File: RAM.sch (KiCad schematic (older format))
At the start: 169 parts, among them J2 JTAG_01x06, J3 Conn_01x03_Male, U10 W25Q128JVS, U11 TPS62823DLC, U12 TPS62823DLC, U13 TPS62823DLC, U14 TPS62823DLC, U15 TPS62823DLC, U16 TPS62823DLC, U2 XC7K160T-FFG676, U3 IS43TR16512B-125KBLI, U4 IS43TR16512B-125KBLI, U5 TPS51200DRC, U6 KSZ9031RNXCA, U7 TUSB1310ZAY, U8 TC358778XBG, U9 SiI9022A, Y1 ABM8G-25.000MHZ-18-D2Y-T, Y2 ABM8G-20.000MHZ-18-D2Y-T

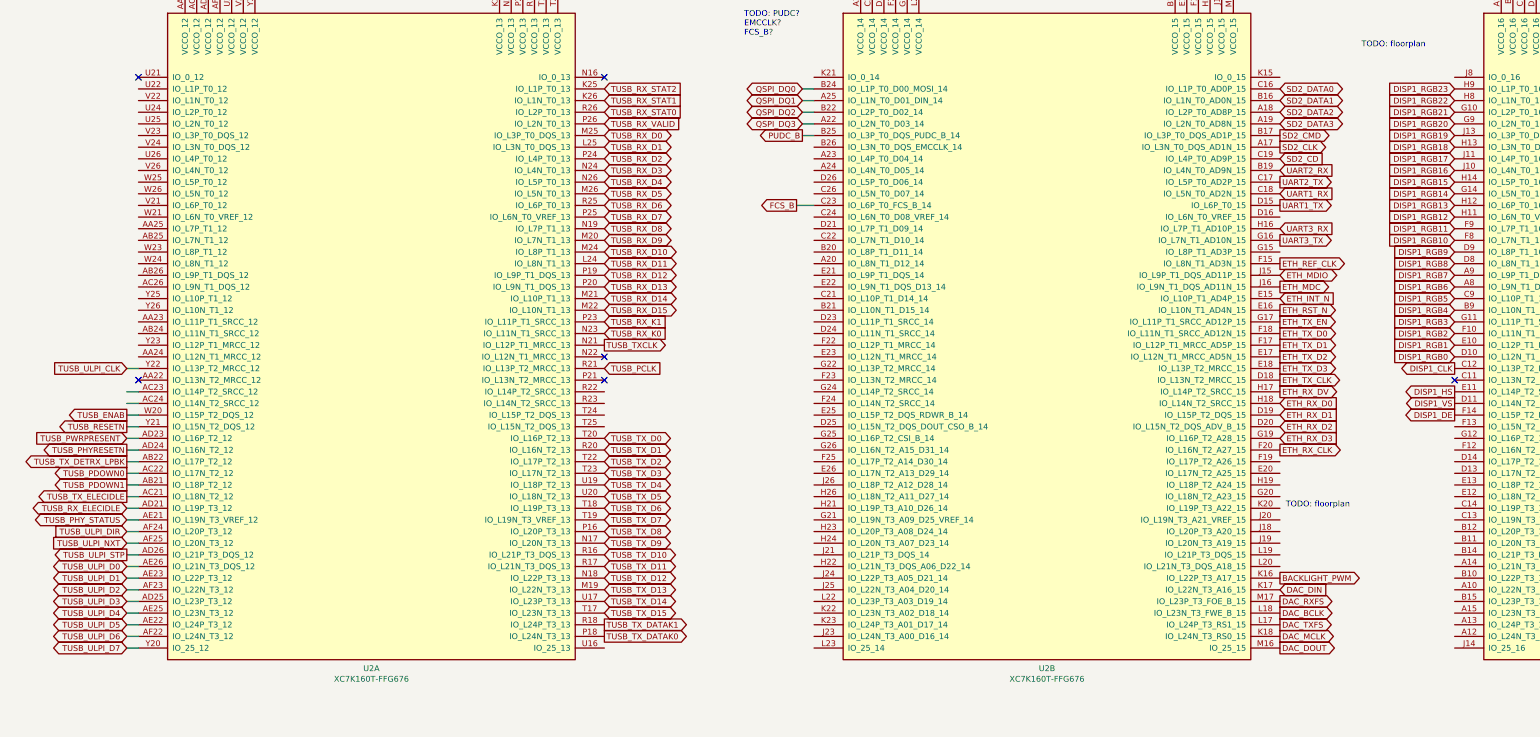
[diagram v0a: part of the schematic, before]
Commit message: more routing, esp. ethernet
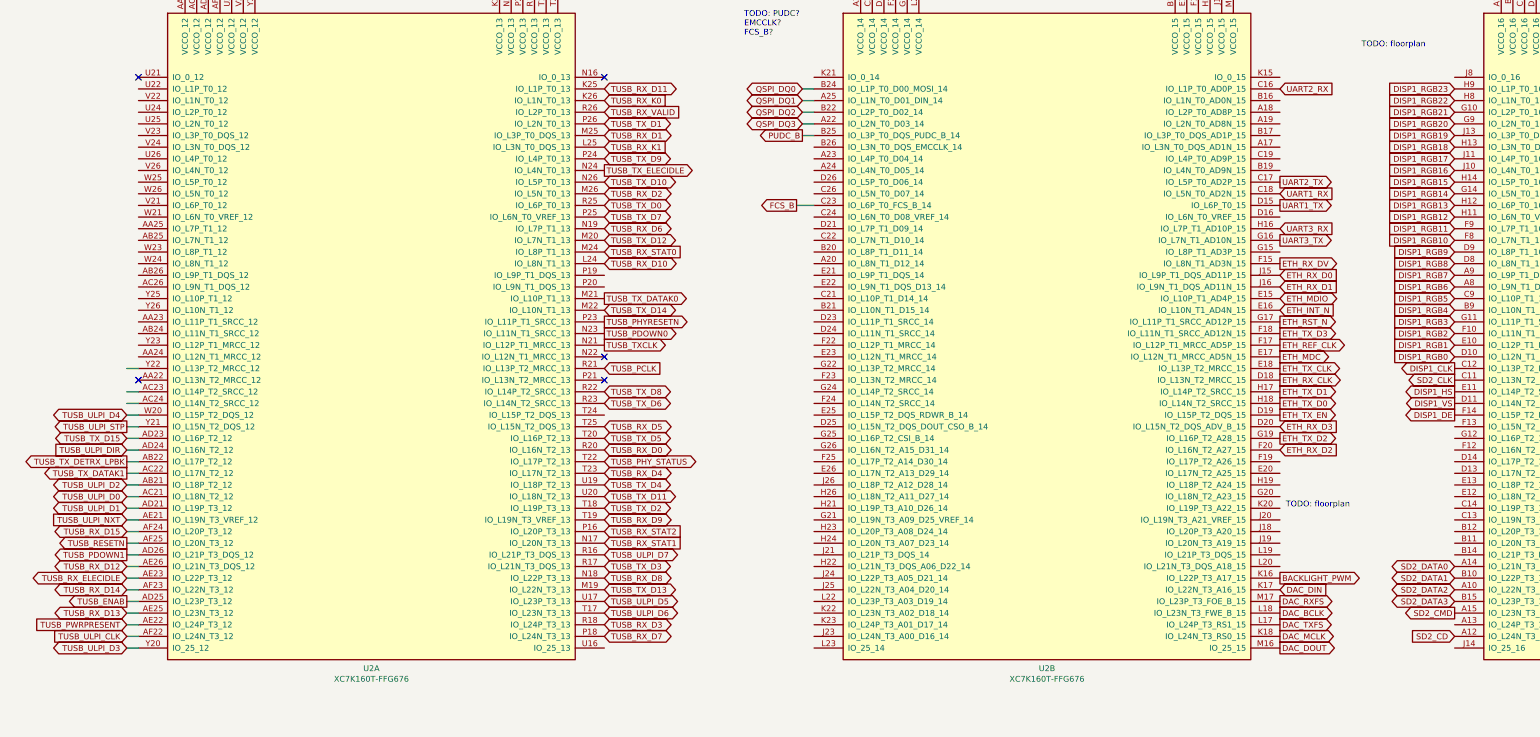
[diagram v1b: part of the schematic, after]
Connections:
- net ETH_INT_N: now also U2.E16 (IO_L10N_T1_AD4N_15); no longer U2.E15 (IO_L10P_T1_AD4P_15)
- net ETH_MDC: now also U2.E17 (IO_L12N_T1_MRCC_AD5N_15); no longer U2.J16 (IO_L9N_T1_DQS_AD11N_15)
- net ETH_MDIO: now also U2.E15 (IO_L10P_T1_AD4P_15); no longer U2.J15 (IO_L9P_T1_DQS_AD11P_15)
- net ETH_REF_CLK: now also U2.F17 (IO_L12P_T1_MRCC_AD5P_15); no longer U2.F15 (IO_L8N_T1_AD3N_15)
- net ETH_RST_N: now also U2.G17 (IO_L11P_T1_SRCC_AD12P_15); no longer U2.E16 (IO_L10N_T1_AD4N_15)
- net ETH_RX_CLK: now also U2.D18 (IO_L13N_T2_MRCC_15); no longer U2.F20 (IO_L16N_T2_A27_15)
- net ETH_RX_D0: now also U2.J15 (IO_L9P_T1_DQS_AD11P_15); no longer U2.H18 (IO_L14N_T2_SRCC_15)
- net ETH_RX_D1: now also U2.J16 (IO_L9N_T1_DQS_AD11N_15); no longer U2.D19 (IO_L15P_T2_DQS_15)
- net ETH_RX_D2: now also U2.F20 (IO_L16N_T2_A27_15); no longer U2.D20 (IO_L15N_T2_DQS_ADV_B_15)
- net ETH_RX_D3: now also U2.D20 (IO_L15N_T2_DQS_ADV_B_15); no longer U2.G19 (IO_L16P_T2_A28_15)
- net ETH_RX_DV: now also U2.F15 (IO_L8N_T1_AD3N_15); no longer U2.H17 (IO_L14P_T2_SRCC_15)
- net ETH_TX_CLK: now also U2.E18 (IO_L13P_T2_MRCC_15); no longer U2.D18 (IO_L13N_T2_MRCC_15)
- net ETH_TX_D0: now also U2.H18 (IO_L14N_T2_SRCC_15); no longer U2.F18 (IO_L11N_T1_SRCC_AD12N_15)
- net ETH_TX_D1: now also U2.H17 (IO_L14P_T2_SRCC_15); no longer U2.F17 (IO_L12P_T1_MRCC_AD5P_15)
- net ETH_TX_D2: now also U2.G19 (IO_L16P_T2_A28_15); no longer U2.E17 (IO_L12N_T1_MRCC_AD5N_15)
- net ETH_TX_D3: now also U2.F18 (IO_L11N_T1_SRCC_AD12N_15); no longer U2.E18 (IO_L13P_T2_MRCC_15)
- net ETH_TX_EN: now also U2.D19 (IO_L15P_T2_DQS_15); no longer U2.G17 (IO_L11P_T1_SRCC_AD12P_15)
- net SD2_CD: now also U2.A12 (IO_L24N_T3_16); no longer U2.C19 (IO_L4P_T0_AD9P_15)
- net SD2_CLK: now also U2.C11 (IO_L13N_T2_MRCC_16); no longer U2.A17 (IO_L3N_T0_DQS_AD1N_15)
- net SD2_CMD: now also U2.A15 (IO_L23N_T3_16); no longer U2.B17 (IO_L3P_T0_DQS_AD1P_15)
- net SD2_DATA0: now also U2.A14 (IO_L21N_T3_DQS_16); no longer U2.C16 (IO_L1P_T0_AD0P_15)
- net SD2_DATA1: now also U2.B10 (IO_L22P_T3_16); no longer U2.B16 (IO_L1N_T0_AD0N_15)
- net SD2_DATA2: now also U2.A10 (IO_L22N_T3_16); no longer U2.A18 (IO_L2P_T0_AD8P_15)
- net SD2_DATA3: now also U2.B15 (IO_L23P_T3_16); no longer U2.A19 (IO_L2N_T0_AD8N_15)
- net TUSB_ENAB: now also U2.AD25 (IO_L23P_T3_12); no longer U2.W20 (IO_L15P_T2_DQS_12)
- net TUSB_PDOWN0: now also U2.N23 (IO_L11N_T1_SRCC_13); no longer U2.AC22 (IO_L17N_T2_12)
- net TUSB_PDOWN1: now also U2.AD26 (IO_L21P_T3_DQS_12); no longer U2.AB21 (IO_L18P_T2_12)
- net TUSB_PHYRESETN: now also U2.P23 (IO_L11P_T1_SRCC_13); no longer U2.AD24 (IO_L16N_T2_12)
- net TUSB_PHY_STATUS: now also U2.T22 (IO_L17P_T2_13); no longer U2.AE21 (IO_L19N_T3_VREF_12)
- net TUSB_PWRPRESENT: now also U2.AE22 (IO_L24P_T3_12); no longer U2.AD23 (IO_L16P_T2_12)
- net TUSB_RESETN: now also U2.AF25 (IO_L20N_T3_12); no longer U2.Y21 (IO_L15N_T2_DQS_12)
- net TUSB_RX_D0: now also U2.R20 (IO_L16N_T2_13); no longer U2.M25 (IO_L3P_T0_DQS_13)
- net TUSB_RX_D1: now also U2.M25 (IO_L3P_T0_DQS_13); no longer U2.L25 (IO_L3N_T0_DQS_13)
- net TUSB_RX_D10: now also U2.L24 (IO_L8N_T1_13); no longer U2.M24 (IO_L8P_T1_13)
- net TUSB_RX_D11: now also U2.K25 (IO_L1P_T0_13); no longer U2.L24 (IO_L8N_T1_13)
- net TUSB_RX_D12: now also U2.AE26 (IO_L21N_T3_DQS_12); no longer U2.P19 (IO_L9P_T1_DQS_13)
- net TUSB_RX_D13: now also U2.AE25 (IO_L23N_T3_12); no longer U2.P20 (IO_L9N_T1_DQS_13)
- net TUSB_RX_D14: now also U2.AF23 (IO_L22N_T3_12); no longer U2.M21 (IO_L10P_T1_13)
- net TUSB_RX_D15: now also U2.AF24 (IO_L20P_T3_12); no longer U2.M22 (IO_L10N_T1_13)
- net TUSB_RX_D2: now also U2.M26 (IO_L5N_T0_13); no longer U2.P24 (IO_L4P_T0_13)
- net TUSB_RX_D3: now also U2.R18 (IO_L24P_T3_13); no longer U2.N24 (IO_L4N_T0_13)
- net TUSB_RX_D4: now also U2.T23 (IO_L17N_T2_13); no longer U2.N26 (IO_L5P_T0_13)
- net TUSB_RX_D5: now also U2.T25 (IO_L15N_T2_DQS_13); no longer U2.M26 (IO_L5N_T0_13)
- net TUSB_RX_D6: now also U2.N19 (IO_L7P_T1_13); no longer U2.R25 (IO_L6P_T0_13)
- net TUSB_RX_D7: now also U2.P18 (IO_L24N_T3_13); no longer U2.P25 (IO_L6N_T0_VREF_13)
- net TUSB_RX_D8: now also U2.N18 (IO_L22P_T3_13); no longer U2.N19 (IO_L7P_T1_13)
- net TUSB_RX_D9: now also U2.T19 (IO_L19N_T3_VREF_13); no longer U2.M20 (IO_L7N_T1_13)
- net TUSB_RX_ELECIDLE: now also U2.AE23 (IO_L22P_T3_12); no longer U2.AD21 (IO_L19P_T3_12)
- net TUSB_RX_K0: now also U2.K26 (IO_L1N_T0_13); no longer U2.N23 (IO_L11N_T1_SRCC_13)
- net TUSB_RX_K1: now also U2.L25 (IO_L3N_T0_DQS_13); no longer U2.P23 (IO_L11P_T1_SRCC_13)
- net TUSB_RX_STAT0: now also U2.M24 (IO_L8P_T1_13); no longer U2.R26 (IO_L2P_T0_13)
- net TUSB_RX_STAT1: now also U2.N17 (IO_L20N_T3_13); no longer U2.K26 (IO_L1N_T0_13)
- net TUSB_RX_STAT2: now also U2.P16 (IO_L20P_T3_13); no longer U2.K25 (IO_L1P_T0_13)
- net TUSB_RX_VALID: now also U2.R26 (IO_L2P_T0_13); no longer U2.P26 (IO_L2N_T0_13)
- net TUSB_TX_D0: now also U2.R25 (IO_L6P_T0_13); no longer U2.T20 (IO_L16P_T2_13)
- net TUSB_TX_D1: now also U2.P26 (IO_L2N_T0_13); no longer U2.R20 (IO_L16N_T2_13)
- net TUSB_TX_D10: now also U2.N26 (IO_L5P_T0_13); no longer U2.R16 (IO_L21P_T3_DQS_13)
- net TUSB_TX_D11: now also U2.U20 (IO_L18N_T2_13); no longer U2.R17 (IO_L21N_T3_DQS_13)
- net TUSB_TX_D12: now also U2.M20 (IO_L7N_T1_13); no longer U2.N18 (IO_L22P_T3_13)
- net TUSB_TX_D14: now also U2.M22 (IO_L10N_T1_13); no longer U2.U17 (IO_L23P_T3_13)
- net TUSB_TX_D15: now also U2.AD23 (IO_L16P_T2_12); no longer U2.T17 (IO_L23N_T3_13)
- net TUSB_TX_D2: now also U2.T18 (IO_L19P_T3_13); no longer U2.T22 (IO_L17P_T2_13)
- net TUSB_TX_D3: now also U2.R17 (IO_L21N_T3_DQS_13); no longer U2.T23 (IO_L17N_T2_13)
- net TUSB_TX_D5: now also U2.T20 (IO_L16P_T2_13); no longer U2.U20 (IO_L18N_T2_13)
- net TUSB_TX_D6: now also U2.R23 (IO_L14N_T2_SRCC_13); no longer U2.T18 (IO_L19P_T3_13)
- net TUSB_TX_D7: now also U2.P25 (IO_L6N_T0_VREF_13); no longer U2.T19 (IO_L19N_T3_VREF_13)
- net TUSB_TX_D8: now also U2.R22 (IO_L14P_T2_SRCC_13); no longer U2.P16 (IO_L20P_T3_13)
- net TUSB_TX_D9: now also U2.P24 (IO_L4P_T0_13); no longer U2.N17 (IO_L20N_T3_13)
- net TUSB_TX_DATAK0: now also U2.M21 (IO_L10P_T1_13); no longer U2.P18 (IO_L24N_T3_13)
- net TUSB_TX_DATAK1: now also U2.AC22 (IO_L17N_T2_12); no longer U2.R18 (IO_L24P_T3_13)
- net TUSB_TX_ELECIDLE: now also U2.N24 (IO_L4N_T0_13); no longer U2.AC21 (IO_L18N_T2_12)
- net TUSB_ULPI_CLK: now also U2.AF22 (IO_L24N_T3_12); no longer U2.Y22 (IO_L13P_T2_MRCC_12)
- net TUSB_ULPI_D0: now also U2.AC21 (IO_L18N_T2_12); no longer U2.AE26 (IO_L21N_T3_DQS_12)
- net TUSB_ULPI_D1: now also U2.AD21 (IO_L19P_T3_12); no longer U2.AE23 (IO_L22P_T3_12)
- net TUSB_ULPI_D2: now also U2.AB21 (IO_L18P_T2_12); no longer U2.AF23 (IO_L22N_T3_12)
- net TUSB_ULPI_D3: now also U2.Y20 (IO_25_12); no longer U2.AD25 (IO_L23P_T3_12)
- net TUSB_ULPI_D4: now also U2.W20 (IO_L15P_T2_DQS_12); no longer U2.AE25 (IO_L23N_T3_12)
- net TUSB_ULPI_D5: now also U2.U17 (IO_L23P_T3_13); no longer U2.AE22 (IO_L24P_T3_12)
- net TUSB_ULPI_D6: now also U2.T17 (IO_L23N_T3_13); no longer U2.AF22 (IO_L24N_T3_12)
- net TUSB_ULPI_D7: now also U2.R16 (IO_L21P_T3_DQS_13); no longer U2.Y20 (IO_25_12)
- net TUSB_ULPI_DIR: now also U2.AD24 (IO_L16N_T2_12); no longer U2.AF24 (IO_L20P_T3_12)
- net TUSB_ULPI_NXT: now also U2.AE21 (IO_L19N_T3_VREF_12); no longer U2.AF25 (IO_L20N_T3_12)
- net TUSB_ULPI_STP: now also U2.Y21 (IO_L15N_T2_DQS_12); no longer U2.AD26 (IO_L21P_T3_DQS_12)
- net UART2_RX: now also U2.C16 (IO_L1P_T0_AD0P_15); no longer U2.B19 (IO_L4N_T0_AD9N_15)
- no-connect marks 23 -> 22
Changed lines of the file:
@@
 Text Notes 14800 14850 0    50   ~ 0
 TODO: bank 14 config pins
-Text GLabel 11300 2700 2    50   Output ~ 0
+Text GLabel 12800 4700 0    50   Output ~ 0
 SD2_CLK
-Text GLabel 11300 2600 2    50   Output ~ 0
+Text GLabel 12800 6700 0    50   Output ~ 0
 SD2_CMD
-Text GLabel 11300 2500 2    50   BiDi ~ 0
+Text GLabel 12800 6600 0    50   BiDi ~ 0
 SD2_DATA3
-Text GLabel 11300 2400 2    50   BiDi ~ 0
+Text GLabel 12800 6500 0    50   BiDi ~ 0
 SD2_DATA2
-Text GLabel 11300 2300 2    50   BiDi ~ 0
+Text GLabel 12800 6400 0    50   BiDi ~ 0
 SD2_DATA1
-Text GLabel 11300 2200 2    50   BiDi ~ 0
+Text GLabel 12800 6300 0    50   BiDi ~ 0
 SD2_DATA0
 Text GLabel 11300 6900 2    50   Output ~ 0
@@
 Wire Wire Line
 	18250 9950 18650 9950
-Text GLabel 11300 2900 2    50   Input ~ 0
+Text GLabel 11300 2200 2    50   Input ~ 0
 UART2_RX
 Text GLabel 11300 3000 2    50   Output ~ 0
@@
 Text GLabel 11300 3200 2    50   Output ~ 0
 UART1_TX
-Text GLabel 11300 2800 2    50   Input ~ 0
+Text GLabel 12800 6900 0    50   Input ~ 0
 SD2_CD
 Text GLabel 11300 3400 2    50   Input ~ 0
@@
 Wire Wire Line
 	38250 11900 38400 11900
-Text GLabel 11300 3700 2    50   Output ~ 0
+Text GLabel 11300 4400 2    50   Output ~ 0
 ETH_REF_CLK
-Text GLabel 11300 3800 2    50   BiDi ~ 0
+Text GLabel 11300 4000 2    50   BiDi ~ 0
 ETH_MDIO
-Text GLabel 11300 3900 2    50   Output ~ 0
+Text GLabel 11300 4500 2    50   Output ~ 0
 ETH_MDC
-Text GLabel 11300 4000 2    50   Input ~ 0
+Text GLabel 11300 4100 2    50   Input ~ 0
 ETH_INT_N
-Text GLabel 11300 4900 2    50   Input ~ 0
+Text GLabel 11300 3800 2    50   Input ~ 0
 ETH_RX_D0
-Text GLabel 11300 5000 2    50   Input ~ 0
+Text GLabel 11300 3900 2    50   Input ~ 0
 ETH_RX_D1
-Text GLabel 11300 5100 2    50   Input ~ 0
+Text GLabel 11300 5300 2    50   Input ~ 0
 ETH_RX_D2
-Text GLabel 11300 5200 2    50   Input ~ 0
+Text GLabel 11300 5100 2    50   Input ~ 0
 ETH_RX_D3
-Text GLabel 11300 4800 2    50   Output ~ 0
+Text GLabel 11300 3700 2    50   Output ~ 0
 ETH_RX_DV
-Text GLabel 11300 4300 2    50   Output ~ 0
+Text GLabel 11300 4900 2    50   Output ~ 0
 ETH_TX_D0
-Text GLabel 11300 4400 2    50   Output ~ 0
+Text GLabel 11300 4800 2    50   Output ~ 0
 ETH_TX_D1
-Text GLabel 11300 4500 2    50   Output ~ 0
+Text GLabel 11300 5200 2    50   Output ~ 0
 ETH_TX_D2
-Text GLabel 11300 4600 2    50   Output ~ 0
+Text GLabel 11300 4300 2    50   Output ~ 0
 ETH_TX_D3
-Text GLabel 11300 4700 2    50   Output ~ 0
+Text GLabel 11300 4600 2    50   Output ~ 0
 ETH_TX_CLK
-Text GLabel 11300 4200 2    50   Output ~ 0
+Text GLabel 11300 5000 2    50   Output ~ 0
 ETH_TX_EN
-Text GLabel 11300 4100 2    50   Output ~ 0
+Text GLabel 11300 4200 2    50   Output ~ 0
 ETH_RST_N
 Text GLabel 35450 11600 0    50   Input ~ 0
@@
 Wire Wire Line
 	35450 11600 35650 11600
-Text GLabel 11300 5300 2    50   Output ~ 0
+Text GLabel 11300 4700 2    50   Output ~ 0
 ETH_RX_CLK
 Text Notes 11350 5800 0    50   ~ 0
@@
 Wire Wire Line
 	5100 21700 4950 21700
-Text GLabel 5500 5200 2    50   BiDi ~ 0
+Text GLabel 5500 3200 2    50   BiDi ~ 0
 TUSB_TX_D0
-Text GLabel 5500 5300 2    50   BiDi ~ 0
+Text GLabel 5500 2500 2    50   BiDi ~ 0
 TUSB_TX_D1
-Text GLabel 5500 5400 2    50   BiDi ~ 0
+Text GLabel 5500 5800 2    50   BiDi ~ 0
 TUSB_TX_D2
-Text GLabel 5500 5500 2    50   BiDi ~ 0
+Text GLabel 5500 6300 2    50   BiDi ~ 0
 TUSB_TX_D3
 Text GLabel 5500 5600 2    50   BiDi ~ 0
 TUSB_TX_D4
-Text GLabel 5500 5700 2    50   BiDi ~ 0
-TUSB_TX_D5
-Text GLabel 5500 5800 2    50   BiDi ~ 0
+Text GLabel 5500 4900 2    50   BiDi ~ 0
 TUSB_TX_D6
-Text GLabel 5500 5900 2    50   BiDi ~ 0
+Text GLabel 5500 3300 2    50   BiDi ~ 0
 TUSB_TX_D7
-Text GLabel 5500 2600 2    50   BiDi ~ 0
+Text GLabel 5500 5300 2    50   BiDi ~ 0
 TUSB_RX_D0
-Text GLabel 5500 2700 2    50   BiDi ~ 0
+Text GLabel 5500 2600 2    50   BiDi ~ 0
 TUSB_RX_D1
-Text GLabel 5500 2800 2    50   BiDi ~ 0
+Text GLabel 5500 3100 2    50   BiDi ~ 0
 TUSB_RX_D2
-Text GLabel 5500 2900 2    50   BiDi ~ 0
-TUSB_RX_D3
-Text GLabel 5500 3000 2    50   BiDi ~ 0
+Text GLabel 5500 5500 2    50   BiDi ~ 0
 TUSB_RX_D4
-Text GLabel 5500 3100 2    50   BiDi ~ 0
+Text GLabel 5500 5100 2    50   BiDi ~ 0
 TUSB_RX_D5
-Text GLabel 5500 3200 2    50   BiDi ~ 0
+Text GLabel 5500 3400 2    50   BiDi ~ 0
 TUSB_RX_D6
-Text GLabel 5500 3300 2    50   BiDi ~ 0
+Text GLabel 5500 6900 2    50   BiDi ~ 0
 TUSB_RX_D7
-Text GLabel 5500 4100 2    50   BiDi ~ 0
+Text GLabel 1400 6000 0    50   BiDi ~ 0
 TUSB_RX_D15
-Text GLabel 5500 6000 2    50   BiDi ~ 0
+Text GLabel 5500 4800 2    50   BiDi ~ 0
 TUSB_TX_D8
-Text GLabel 5500 6100 2    50   BiDi ~ 0
+Text GLabel 5500 2800 2    50   BiDi ~ 0
 TUSB_TX_D9
-Text GLabel 5500 6200 2    50   BiDi ~ 0
+Text GLabel 5500 3000 2    50   BiDi ~ 0
 TUSB_TX_D10
-Text GLabel 5500 6300 2    50   BiDi ~ 0
+Text GLabel 5500 5700 2    50   BiDi ~ 0
 TUSB_TX_D11
-Text GLabel 5500 6400 2    50   BiDi ~ 0
+Text GLabel 5500 3500 2    50   BiDi ~ 0
 TUSB_TX_D12
 Text GLabel 5500 6500 2    50   BiDi ~ 0
 TUSB_TX_D13
-Text GLabel 5500 6600 2    50   BiDi ~ 0
+Text GLabel 5500 4100 2    50   BiDi ~ 0
 TUSB_TX_D14
-Text GLabel 5500 3400 2    50   BiDi ~ 0
+Text GLabel 5500 6400 2    50   BiDi ~ 0
 TUSB_RX_D8
-Text GLabel 5500 3500 2    50   BiDi ~ 0
+Text GLabel 5500 5900 2    50   BiDi ~ 0
 TUSB_RX_D9
-Text GLabel 5500 3600 2    50   BiDi ~ 0
-TUSB_RX_D10
 Text GLabel 5500 3700 2    50   BiDi ~ 0
+TUSB_RX_D10
+Text GLabel 5500 2200 2    50   BiDi ~ 0
 TUSB_RX_D11
-Text GLabel 5500 3800 2    50   BiDi ~ 0
+Text GLabel 1400 6300 0    50   BiDi ~ 0
 TUSB_RX_D12
-Text GLabel 5500 3900 2    50   BiDi ~ 0
+Text GLabel 1400 6700 0    50   BiDi ~ 0
 TUSB_RX_D13
-Text GLabel 5500 4000 2    50   BiDi ~ 0
+Text GLabel 1400 6500 0    50   BiDi ~ 0
 TUSB_RX_D14
 Text GLabel 2550 22850 0    50   BiDi ~ 0
@@
 Wire Wire Line
 	4850 22650 5100 22650
-Text GLabel 1400 6300 0    50   BiDi ~ 0
+Text GLabel 1400 5700 0    50   BiDi ~ 0
 TUSB_ULPI_D0
 Wire Wire Line
 	1400 6300 1500 6300
-Text GLabel 1400 6500 0    50   BiDi ~ 0
+Text GLabel 1400 5600 0    50   BiDi ~ 0
 TUSB_ULPI_D2
 Wire Wire Line
 	1400 6500 1500 6500
-Text GLabel 1400 6700 0    50   BiDi ~ 0
+Text GLabel 1400 5000 0    50   BiDi ~ 0
 TUSB_ULPI_D4
 Wire Wire Line
 	1400 6700 1500 6700
-Text GLabel 1400 6900 0    50   BiDi ~ 0
+Text GLabel 5500 6700 2    50   BiDi ~ 0
 TUSB_ULPI_D6
 Wire Wire Line
 	1400 6900 1500 6900
-Text GLabel 1400 6400 0    50   BiDi ~ 0
+Text GLabel 1400 5800 0    50   BiDi ~ 0
 TUSB_ULPI_D1
-Text GLabel 1400 6600 0    50   BiDi ~ 0
+Text GLabel 1400 7000 0    50   BiDi ~ 0
 TUSB_ULPI_D3
-Text GLabel 1400 6800 0    50   BiDi ~ 0
-TUSB_ULPI_D5
 Wire Wire Line
 	1400 6400 1500 6400
@@
 Wire Wire Line
 	1400 6800 1500 6800
-Text GLabel 1400 7000 0    50   BiDi ~ 0
+Text GLabel 5500 6200 2    50   BiDi ~ 0
 TUSB_ULPI_D7
 Wire Wire Line
@@
 Wire Wire Line
 	2750 17900 2450 17900
-Text GLabel 5500 2400 2    50   Input ~ 0
+Text GLabel 5500 3600 2    50   Input ~ 0
 TUSB_RX_STAT0
-Text GLabel 5500 2300 2    50   Input ~ 0
-TUSB_RX_STAT1
-Text GLabel 5500 2200 2    50   Input ~ 0
+Text GLabel 5500 6000 2    50   Input ~ 0
 TUSB_RX_STAT2
-Text GLabel 1400 5200 0    50   Input ~ 0
+Text GLabel 1400 6800 0    50   Input ~ 0
 TUSB_PWRPRESENT
-Text GLabel 1400 5300 0    50   Output ~ 0
-TUSB_PHYRESETN
-Text GLabel 1400 5700 0    50   Output ~ 0
+Text GLabel 5500 2900 2    50   Output ~ 0
 TUSB_TX_ELECIDLE
-Text GLabel 1400 5800 0    50   BiDi ~ 0
+Text GLabel 1400 6400 0    50   BiDi ~ 0
 TUSB_RX_ELECIDLE
-Text GLabel 1400 5500 0    50   Output ~ 0
+Text GLabel 5500 4300 2    50   Output ~ 0
 TUSB_PDOWN0
-Text GLabel 1400 5600 0    50   Output ~ 0
+Text GLabel 1400 6200 0    50   Output ~ 0
 TUSB_PDOWN1
-Text GLabel 1400 5900 0    50   BiDi ~ 0
+Text GLabel 5500 5400 2    50   BiDi ~ 0
 TUSB_PHY_STATUS
 Text GLabel 1400 5400 0    50   Output ~ 0
 TUSB_TX_DETRX_LPBK
-Text GLabel 1400 6000 0    50   Input ~ 0
+Text GLabel 1400 5300 0    50   Input ~ 0
 TUSB_ULPI_DIR
-Text GLabel 1400 4600 0    50   Input ~ 0
+Text GLabel 1400 6900 0    50   Input ~ 0
 TUSB_ULPI_CLK
-Text GLabel 1400 6100 0    50   Input ~ 0
+Text GLabel 1400 5900 0    50   Input ~ 0
 TUSB_ULPI_NXT
-Text GLabel 1400 6200 0    50   Output ~ 0
+Text GLabel 1400 5100 0    50   Output ~ 0
 TUSB_ULPI_STP
 Wire Wire Line
@@
 Text GLabel 5500 4600 2    50   Input ~ 0
 TUSB_PCLK
-Text GLabel 5500 2500 2    50   Input ~ 0
+Text GLabel 5500 2400 2    50   Input ~ 0
 TUSB_RX_VALID
-Text GLabel 5500 4300 2    50   Input ~ 0
+Text GLabel 5500 2300 2    50   Input ~ 0
 TUSB_RX_K0
-Text GLabel 5500 4200 2    50   Input ~ 0
+Text GLabel 5500 2700 2    50   Input ~ 0
 TUSB_RX_K1
 Text GLabel 5500 4400 2    50   Output ~ 0
 TUSB_TXCLK
-Text GLabel 5500 6900 2    50   Output ~ 0
-TUSB_TX_DATAK0
-Text GLabel 5500 6800 2    50   Output ~ 0
+Text GLabel 1400 5500 0    50   Output ~ 0
 TUSB_TX_DATAK1
-Text GLabel 5500 6700 2    50   BiDi ~ 0
+Text GLabel 1400 5200 0    50   BiDi ~ 0
 TUSB_TX_D15
 Wire Wire Line
@@
 NoConn ~ 1500 4700
 NoConn ~ 16800 4700
-NoConn ~ 12800 4700
 Text Notes 18350 11750 0    50   ~ 0
 TODO: PCIe clocking
@@
 Wire Wire Line
 	7300 3200 7150 3200
-Text GLabel 1400 5000 0    50   Output ~ 0
+Text GLabel 1400 6600 0    50   Output ~ 0
 TUSB_ENAB
-Text GLabel 1400 5100 0    50   Output ~ 0
+Text GLabel 1400 6100 0    50   Output ~ 0
 TUSB_RESETN
 $Comp
@@
 Text GLabel 16800 3800 2    50   Input ~ 0
 DISP2_RGB18
+Text GLabel 5500 6600 2    50   BiDi ~ 0
+TUSB_ULPI_D5
+Text GLabel 5500 4000 2    50   Output ~ 0
+TUSB_TX_DATAK0
+Text GLabel 5500 4200 2    50   Output ~ 0
+TUSB_PHYRESETN
+Text GLabel 5500 5200 2    50   BiDi ~ 0
+TUSB_TX_D5
+Text GLabel 5500 6800 2    50   BiDi ~ 0
+TUSB_RX_D3
+Text GLabel 5500 6100 2    50   Input ~ 0
+TUSB_RX_STAT1
 $EndSCHEMATC
